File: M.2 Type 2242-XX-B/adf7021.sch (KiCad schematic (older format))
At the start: 46 parts, among them U2 AS193-73, U3 M74VHC1GT04DFT1G, U4 ADF7021BCPZ, X1 FT5HNBPK19.44-T1

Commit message: Schematic updated to STM32F103
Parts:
- C10, C11, C12, C13, C14, C15, C16, C17, C18, C19, C2, C20, C21, C22, C23, C3, C34, C35, C36, C4, C5, C6, C7, C8, C9: footprint Capacitor_SMD:C_0402_1005Metric -> Capacitor_SMD:C_0603_1608Metric
- R1, R2, R3, R4, R5, R6, R7, R8: footprint Resistor_SMD:R_0402_1005Metric -> Resistor_SMD:R_0603_1608Metric
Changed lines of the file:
@@
 Text HLabel 1250 1250 0    50   Input ~ 0
 ANT_SELECT
-Wire Wire Line
-	7250 1500 7250 1750
-Connection ~ 7250 1500
-Wire Wire Line
-	7000 1500 7250 1500
-Wire Wire Line
-	7250 1250 7250 1500
-Wire Wire Line
-	7000 1450 7000 1500
-$Comp
-L power:PWR_FLAG #FLG?
-U 1 1 5DAD197A
-P 7000 1450
-AR Path="/5CA93306/5DAD197A" Ref="#FLG?"  Part="1"
-AR Path="/5CA93143/5DAD197A" Ref="#FLG?"  Part="1"
-AR Path="/5DA4D1CA/5DAD197A" Ref="#FLG?"  Part="1"
-AR Path="/5DA99182/5DAD197A" Ref="#FLG0101"  Part="1"
-AR Path="/5DC39AF2/5DAD197A" Ref="#FLG?"  Part="1"
-AR Path="/5DC39DB3/5DAD197A" Ref="#FLG?"  Part="1"
-AR Path="/5DC39F66/5DAD197A" Ref="#FLG?"  Part="1"
-F 0 "#FLG0101" H 7000 1525 50  0001 C CNN
-F 1 "PWR_FLAG" H 7000 1623 50  0000 C CNN
-F 2 "" H 7000 1450 50  0001 C CNN
-F 3 "~" H 7000 1450 50  0001 C CNN
-	1    7000 1450
-	1    0    0    -1
-$EndComp
 Text Notes 7600 800  0    50   ~ 0
 NOTE: This is to make it easy to hack\nif we need to test with seperate supply.
@@
 F 0 "C8" H 3385 3346 50  0000 R CNN
 F 1 "220pF" H 3385 3255 50  0000 R CNN
-F 2 "Capacitor_SMD:C_0402_1005Metric" H 3538 3150 50  0001 C CNN
+F 2 "Capacitor_SMD:C_0603_1608Metric" H 3538 3150 50  0001 C CNN
 F 3 "~" H 3500 3300 50  0001 C CNN
 	1    3500 3300
@@
 F 0 "C6" H 3365 3346 50  0000 L CNN
 F 1 "10nF" H 3365 3255 50  0000 L CNN
-F 2 "Capacitor_SMD:C_0402_1005Metric" H 3288 3150 50  0001 C CNN
+F 2 "Capacitor_SMD:C_0603_1608Metric" H 3288 3150 50  0001 C CNN
 F 3 "~" H 3250 3300 50  0001 C CNN
 	1    3250 3300
@@
 F 0 "C3" V 1310 2250 50  0000 C CNN
 F 1 "100pF" V 1401 2250 50  0000 C CNN
-F 2 "Capacitor_SMD:C_0402_1005Metric" H 1188 2100 50  0001 C CNN
+F 2 "Capacitor_SMD:C_0603_1608Metric" H 1188 2100 50  0001 C CNN
 F 3 "~" H 1150 2250 50  0001 C CNN
 	1    1150 2250
@@
 F 0 "C2" V 898 2050 50  0000 C CNN
 F 1 "100pF" V 989 2050 50  0000 C CNN
-F 2 "Capacitor_SMD:C_0402_1005Metric" H 1188 1900 50  0001 C CNN
+F 2 "Capacitor_SMD:C_0603_1608Metric" H 1188 1900 50  0001 C CNN
 F 3 "~" H 1150 2050 50  0001 C CNN
 	1    1150 2050
@@
 F 0 "C5" V 2198 2150 50  0000 C CNN
 F 1 "100pF" V 2289 2150 50  0000 C CNN
-F 2 "Capacitor_SMD:C_0402_1005Metric" H 2488 2000 50  0001 C CNN
+F 2 "Capacitor_SMD:C_0603_1608Metric" H 2488 2000 50  0001 C CNN
 F 3 "~" H 2450 2150 50  0001 C CNN
 	1    2450 2150
@@
 F 0 "C19" H 7715 1446 50  0000 L CNN
 F 1 "10nF" H 7715 1355 50  0000 L CNN
-F 2 "Capacitor_SMD:C_0402_1005Metric" H 7638 1250 50  0001 C CNN
+F 2 "Capacitor_SMD:C_0603_1608Metric" H 7638 1250 50  0001 C CNN
 F 3 "~" H 7600 1400 50  0001 C CNN
 	1    7600 1400
@@
 F 0 "C10" V 4298 3050 50  0000 C CNN
 F 1 "100nF" V 4389 3050 50  0000 C CNN
-F 2 "Capacitor_SMD:C_0402_1005Metric" H 4588 2900 50  0001 C CNN
+F 2 "Capacitor_SMD:C_0603_1608Metric" H 4588 2900 50  0001 C CNN
 F 3 "~" H 4550 3050 50  0001 C CNN
 	1    4550 3050
@@
 F 0 "R2" V 4743 3050 50  0000 C CNN
 F 1 "3R9" V 4834 3050 50  0000 C CNN
-F 2 "Resistor_SMD:R_0402_1005Metric" V 4880 3050 50  0001 C CNN
+F 2 "Resistor_SMD:R_0603_1608Metric" V 4880 3050 50  0001 C CNN
 F 3 "~" H 4950 3050 50  0001 C CNN
 	1    4950 3050
@@
 F 0 "C21" H 8465 4746 50  0000 L CNN
 F 1 "100nF" H 8465 4655 50  0000 L CNN
-F 2 "Capacitor_SMD:C_0402_1005Metric" H 8388 4550 50  0001 C CNN
+F 2 "Capacitor_SMD:C_0603_1608Metric" H 8388 4550 50  0001 C CNN
 F 3 "~" H 8350 4700 50  0001 C CNN
 	1    8350 4700
@@
 F 0 "R5" H 5920 1296 50  0000 L CNN
 F 1 "270R" H 5920 1205 50  0000 L CNN
-F 2 "Resistor_SMD:R_0402_1005Metric" V 5780 1250 50  0001 C CNN
+F 2 "Resistor_SMD:R_0603_1608Metric" V 5780 1250 50  0001 C CNN
 F 3 "~" H 5850 1250 50  0001 C CNN
 	1    5850 1250
@@
 F 0 "C23" H 8965 4646 50  0000 L CNN
 F 1 "10nF" H 8965 4555 50  0000 L CNN
-F 2 "Capacitor_SMD:C_0402_1005Metric" H 8888 4450 50  0001 C CNN
+F 2 "Capacitor_SMD:C_0603_1608Metric" H 8888 4450 50  0001 C CNN
 F 3 "~" H 8850 4600 50  0001 C CNN
 	1    8850 4600
@@
 F 0 "C18" H 7015 2846 50  0000 L CNN
 F 1 "22pF" H 7015 2755 50  0000 L CNN
-F 2 "Capacitor_SMD:C_0402_1005Metric" H 6938 2650 50  0001 C CNN
+F 2 "Capacitor_SMD:C_0603_1608Metric" H 6938 2650 50  0001 C CNN
 F 3 "~" H 6900 2800 50  0001 C CNN
 	1    6900 2800
@@
 F 0 "R4" H 5470 1296 50  0000 L CNN
 F 1 "560R" H 5470 1205 50  0000 L CNN
-F 2 "Resistor_SMD:R_0402_1005Metric" V 5330 1250 50  0001 C CNN
+F 2 "Resistor_SMD:R_0603_1608Metric" V 5330 1250 50  0001 C CNN
 F 3 "~" H 5400 1250 50  0001 C CNN
 	1    5400 1250
@@
 F 0 "C16" H 5965 1696 50  0000 L CNN
 F 1 "15nF" H 5965 1605 50  0000 L CNN
-F 2 "Capacitor_SMD:C_0402_1005Metric" H 5888 1500 50  0001 C CNN
+F 2 "Capacitor_SMD:C_0603_1608Metric" H 5888 1500 50  0001 C CNN
 F 3 "~" H 5850 1650 50  0001 C CNN
 	1    5850 1650
@@
 F 0 "C14" H 5515 1696 50  0000 L CNN
 F 1 "470pF" H 5515 1605 50  0000 L CNN
-F 2 "Capacitor_SMD:C_0402_1005Metric" H 5438 1500 50  0001 C CNN
+F 2 "Capacitor_SMD:C_0603_1608Metric" H 5438 1500 50  0001 C CNN
 F 3 "~" H 5400 1650 50  0001 C CNN
 	1    5400 1650
@@
 F 0 "C17" H 6415 1446 50  0000 L CNN
 F 1 "1nF" H 6415 1355 50  0000 L CNN
-F 2 "Capacitor_SMD:C_0402_1005Metric" H 6338 1250 50  0001 C CNN
+F 2 "Capacitor_SMD:C_0603_1608Metric" H 6338 1250 50  0001 C CNN
 F 3 "~" H 6300 1400 50  0001 C CNN
 	1    6300 1400
@@
 F 0 "C20" H 7835 3546 50  0000 R CNN
 F 1 "100nF" H 7835 3455 50  0000 R CNN
-F 2 "Capacitor_SMD:C_0402_1005Metric" H 7988 3350 50  0001 C CNN
+F 2 "Capacitor_SMD:C_0603_1608Metric" H 7988 3350 50  0001 C CNN
 F 3 "~" H 7950 3500 50  0001 C CNN
 	1    7950 3500
@@
 F 0 "C15" V 5548 3050 50  0000 C CNN
 F 1 "22nF" V 5639 3050 50  0000 C CNN
-F 2 "Capacitor_SMD:C_0402_1005Metric" H 5838 2900 50  0001 C CNN
+F 2 "Capacitor_SMD:C_0603_1608Metric" H 5838 2900 50  0001 C CNN
 F 3 "~" H 5800 3050 50  0001 C CNN
 	1    5800 3050
@@
 F 0 "C11" H 4765 3996 50  0000 L CNN
 F 1 "10nF" H 4765 3905 50  0000 L CNN
-F 2 "Capacitor_SMD:C_0402_1005Metric" H 4688 3800 50  0001 C CNN
+F 2 "Capacitor_SMD:C_0603_1608Metric" H 4688 3800 50  0001 C CNN
 F 3 "~" H 4650 3950 50  0001 C CNN
 	1    4650 3950
@@
 F 0 "R6" V 7700 4250 50  0000 C CNN
 F 1 "1K" V 7750 4400 50  0000 C CNN
-F 2 "Resistor_SMD:R_0402_1005Metric" V 7630 4250 50  0001 C CNN
+F 2 "Resistor_SMD:R_0603_1608Metric" V 7630 4250 50  0001 C CNN
 F 3 "~" H 7700 4250 50  0001 C CNN
 	1    7700 4250
@@
 F 0 "R7" V 7850 4150 50  0000 C CNN
 F 1 "1K" V 7900 4300 50  0000 C CNN
-F 2 "Resistor_SMD:R_0402_1005Metric" V 7780 4150 50  0001 C CNN
+F 2 "Resistor_SMD:R_0603_1608Metric" V 7780 4150 50  0001 C CNN
 F 3 "~" H 7850 4150 50  0001 C CNN
 	1    7850 4150
@@
 F 0 "R8" V 7950 4050 50  0000 C CNN
 F 1 "1K" V 8000 4200 50  0000 C CNN
-F 2 "Resistor_SMD:R_0402_1005Metric" V 7880 4050 50  0001 C CNN
+F 2 "Resistor_SMD:R_0603_1608Metric" V 7880 4050 50  0001 C CNN
 F 3 "~" H 7950 4050 50  0001 C CNN
 	1    7950 4050
@@
 F 0 "C22" H 8615 3246 50  0000 L CNN
 F 1 "10nF" H 8615 3155 50  0000 L CNN
-F 2 "Capacitor_SMD:C_0402_1005Metric" H 8538 3050 50  0001 C CNN
+F 2 "Capacitor_SMD:C_0603_1608Metric" H 8538 3050 50  0001 C CNN
 F 3 "~" H 8500 3200 50  0001 C CNN
 	1    8500 3200
@@
 F 0 "C12" H 4636 5846 50  0000 R CNN
 F 1 "10nF" H 4636 5755 50  0000 R CNN
-F 2 "Capacitor_SMD:C_0402_1005Metric" H 4788 5650 50  0001 C CNN
+F 2 "Capacitor_SMD:C_0603_1608Metric" H 4788 5650 50  0001 C CNN
 F 3 "~" H 4750 5800 50  0001 C CNN
 	1    4750 5800
@@
 F 0 "R3" H 5020 5346 50  0000 L CNN
 F 1 "3K6" H 5020 5255 50  0000 L CNN
-F 2 "Resistor_SMD:R_0402_1005Metric" V 4880 5300 50  0001 C CNN
+F 2 "Resistor_SMD:R_0603_1608Metric" V 4880 5300 50  0001 C CNN
 F 3 "~" H 4950 5300 50  0001 C CNN
 	1    4950 5300
@@
 F 0 "C13" H 5315 5846 50  0000 L CNN
 F 1 "100nF" H 5315 5755 50  0000 L CNN
-F 2 "Capacitor_SMD:C_0402_1005Metric" H 5238 5650 50  0001 C CNN
+F 2 "Capacitor_SMD:C_0603_1608Metric" H 5238 5650 50  0001 C CNN
 F 3 "~" H 5200 5800 50  0001 C CNN
 	1    5200 5800
@@
 F 0 "R1" H 4220 5196 50  0000 L CNN
 F 1 "1K1" H 4220 5105 50  0000 L CNN
-F 2 "Resistor_SMD:R_0402_1005Metric" V 4080 5150 50  0001 C CNN
+F 2 "Resistor_SMD:R_0603_1608Metric" V 4080 5150 50  0001 C CNN
 F 3 "~" H 4150 5150 50  0001 C CNN
 	1    4150 5150
@@
 F 0 "C9" H 3665 5196 50  0000 L CNN
 F 1 "11pF" H 3665 5105 50  0000 L CNN
-F 2 "Capacitor_SMD:C_0402_1005Metric" H 3588 5000 50  0001 C CNN
+F 2 "Capacitor_SMD:C_0603_1608Metric" H 3588 5000 50  0001 C CNN
 F 3 "~" H 3550 5150 50  0001 C CNN
 	1    3550 5150
@@
 F 0 "C7" V 3300 4400 50  0000 C CNN
 F 1 "11pF" V 3400 4400 50  0000 C CNN
-F 2 "Capacitor_SMD:C_0402_1005Metric" H 3288 4400 50  0001 C CNN
+F 2 "Capacitor_SMD:C_0603_1608Metric" H 3288 4400 50  0001 C CNN
 F 3 "~" H 3250 4550 50  0001 C CNN
 	1    3250 4550
@@
 F 0 "C36" V 3750 4200 50  0000 C CNN
 F 1 "11pF" V 3850 4200 50  0000 C CNN
-F 2 "Capacitor_SMD:C_0402_1005Metric" H 3738 4200 50  0001 C CNN
+F 2 "Capacitor_SMD:C_0603_1608Metric" H 3738 4200 50  0001 C CNN
 F 3 "~" H 3700 4350 50  0001 C CNN
 	1    3700 4350
@@
 F 0 "C35" H 2665 4846 50  0000 L CNN
 F 1 "C" H 2665 4755 50  0000 L CNN
-F 2 "Capacitor_SMD:C_0402_1005Metric" H 2588 4650 50  0001 C CNN
+F 2 "Capacitor_SMD:C_0603_1608Metric" H 2588 4650 50  0001 C CNN
 F 3 "~" H 2550 4800 50  0001 C CNN
 	1    2550 4800
@@
 F 0 "C34" H 2165 4846 50  0000 L CNN
 F 1 "6.8pF" H 2165 4755 50  0000 L CNN
-F 2 "Capacitor_SMD:C_0402_1005Metric" H 2088 4650 50  0001 C CNN
+F 2 "Capacitor_SMD:C_0603_1608Metric" H 2088 4650 50  0001 C CNN
 F 3 "~" H 2050 4800 50  0001 C CNN
 	1    2050 4800
@@
 F 0 "C4" H 1665 4846 50  0000 L CNN
 F 1 "C" H 1665 4755 50  0000 L CNN
-F 2 "Capacitor_SMD:C_0402_1005Metric" H 1588 4650 50  0001 C CNN
+F 2 "Capacitor_SMD:C_0603_1608Metric" H 1588 4650 50  0001 C CNN
 F 3 "~" H 1550 4800 50  0001 C CNN
 	1    1550 4800
@@
 Wire Wire Line
 	2100 2250 3350 2250
+Wire Wire Line
+	7250 1250 7250 1750
 $EndSCHEMATC

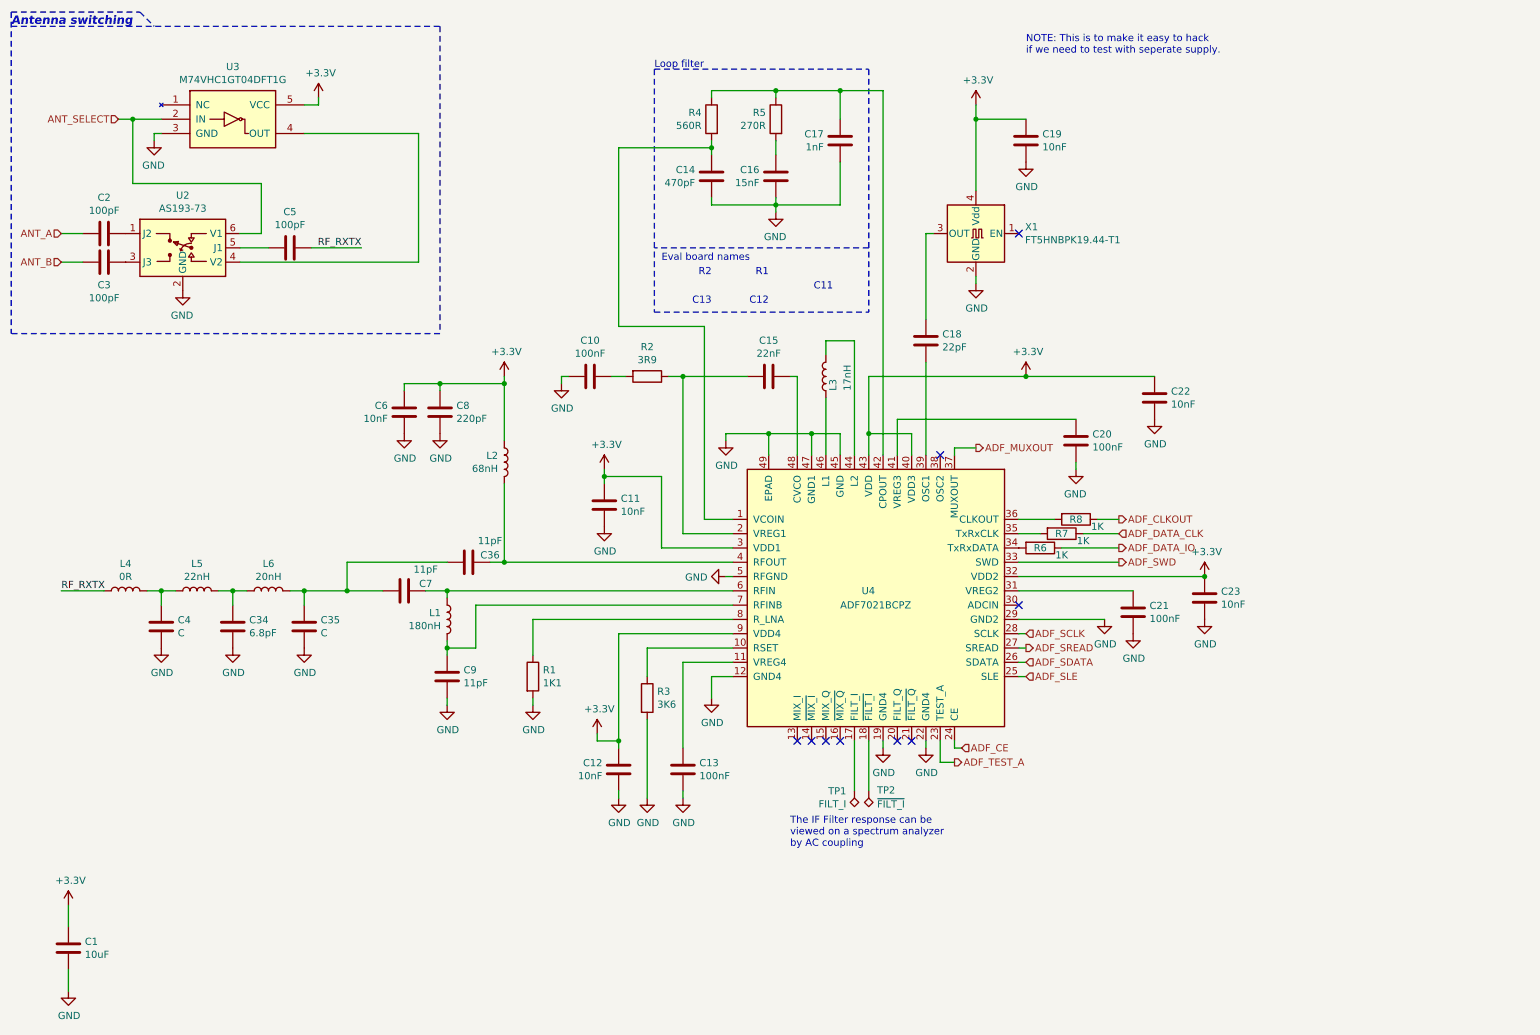
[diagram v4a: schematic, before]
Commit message: Almost everything placed
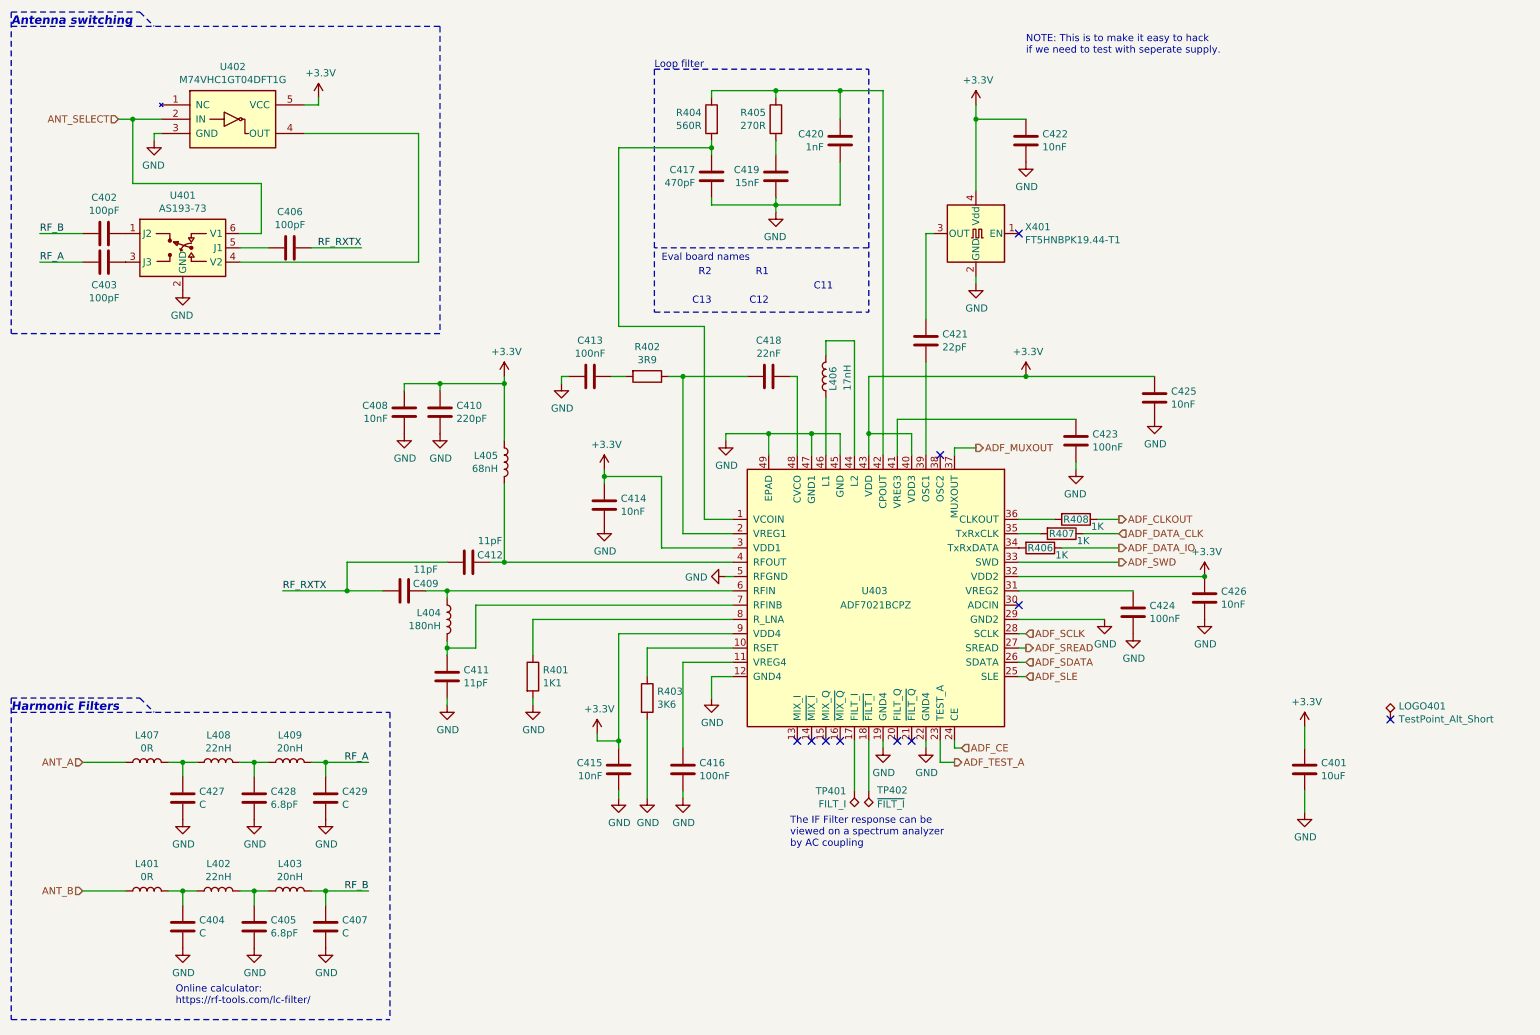
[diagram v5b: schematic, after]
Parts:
- added C427, C429: C, Capacitor_SMD:C_0603_1608Metric, symbol Device:C
- added C428: 6.8pF, Capacitor_SMD:C_0603_1608Metric, symbol Device:C
- added L407: 0R, Inductor_SMD:L_0603_1608Metric, symbol Device:L
- added L408: 22nH, Inductor_SMD:L_0603_1608Metric, symbol Device:L
- added L409: 20nH, Inductor_SMD:L_0603_1608Metric, symbol Device:L
- added LOGO401: TestPoint_Alt_Short, aausat:KiCad-Logo_Back, symbol aausat:TestPoint_Alt_Short
- C401: renamed from C1; footprint Capacitor_SMD:C_0603_1608Metric -> Capacitor_SMD:C_0805_2012Metric
- TP401: renamed from TP1; footprint TestPoint:TestPoint_Pad_D1.5mm -> aausat:TestPad
- TP402: renamed from TP2; footprint TestPoint:TestPoint_Pad_D1.5mm -> aausat:TestPad
- renumbered C2 to C402, C3 to C403, C4 to C404, C34 to C405, C5 to C406, C35 to C407, C6 to C408, C7 to C409, C8 to C410, C9 to C411, C36 to C412, C10 to C413, C11 to C414, C12 to C415, C13 to C416, C14 to C417, C15 to C418, C16 to C419, C17 to C420, C18 to C421, C19 to C422, C20 to C423, C21 to C424, C22 to C425, C23 to C426, L4 to L401, L5 to L402, L6 to L403, L1 to L404, L2 to L405, L3 to L406, R1 to R401, R2 to R402, R3 to R403, R4 to R404, R5 to R405, R6 to R406, R7 to R407, R8 to R408, U2 to U401, U3 to U402, U4 to U403, X1 to X401
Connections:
- net ANT_A: now also L407.1; no longer C402.2
- net ANT_B: now also L401.1; no longer C403.2
- net GND: now also C427.2, C428.2, C429.2
- net RF_RXTX: now also C409.1, C412.1; no longer L401.1
- net RF_B: now reaches C407.1, L403.2
- net RF_B: now also C402.2; no longer C409.1, C412.1
- new net: C428.1, L408.2, L409.1
- new net: C427.1, L407.2, L408.1
- new net RF_A: C403.2, C429.1, L409.2
- no-connect marks 9 -> 10
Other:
- note added: "Harmonic Filters"
- note added: "Online calculator:\nhttps://rf-tools.com/lc-filter/"
- moved on the sheet: C401, C404, C405, C407, L401, L402, L403
